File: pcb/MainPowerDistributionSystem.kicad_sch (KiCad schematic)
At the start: 12 parts, among them J2 PREC040DBAN-M71RC, U1 TPS22810DRV, U2 D24V7F5, U3 D24V7F3

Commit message: Renamed symbol and footprint `StackConnector` to `MainStackConnector`.
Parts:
- J1: footprint pcb:StackConnector -> pcb:MainStackConnector; symbol StackConnector:StackConnector -> MainStackConnector:MainStackConnector
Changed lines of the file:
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@@
 	)
 	(symbol
-		(lib_id "StackConnector:StackConnector")
+		(lib_id "MainStackConnector:MainStackConnector")
 		(at 461.01 69.85 0)
 		(unit 1)
@@
 			)
 		)
-		(property "Footprint" "pcb:StackConnector"
+		(property "Footprint" "pcb:MainStackConnector"
 			(at 459.74 69.85 0)
 			(effects

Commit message: Removed stepper motor drivers from `MainPowerDistributionSystem`.
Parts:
- removed JP1: Jumper_2_Bridged, Jumper:SolderJumper-2_P1.3mm_Open_RoundedPad1.0x1.5mm, symbol Jumper:Jumper_2_Bridged
- removed JP2: SolderJumper_2_Open, Jumper:SolderJumper-2_P1.3mm_Open_RoundedPad1.0x1.5mm, symbol Jumper:SolderJumper_2_Open
- removed R2: 1k, Resistor_SMD:R_1206_3216Metric_Pad1.30x1.75mm_HandSolder, symbol Device:R
- removed R3: 20k, Resistor_SMD:R_1206_3216Metric_Pad1.30x1.75mm_HandSolder, symbol Device:R
- removed TP1, TP2: TestPoint, TestPoint:TestPoint_Pad_1.0x1.0mm, symbol Connector:TestPoint
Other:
- removed sheet Stepper Motor Driver - X
- removed sheet Stepper Motor Driver - Y
- removed sheet Stepper Motor Driver - Z
- note removed: "@/pg 14/sec 3.4/`TMC2209`."
- note removed: "@/pg 20/fig 4.1/`TMC2209`."
- note removed: "Stepper Motor Drivers."
- note removed: "VREF is used for current scaling or something, but I don't think we'll need it; can be left floating according to example application diagram. @/pg 4/fig 1.1/`TMC2209`."
- moved on the sheet: J1, J2, R1, U1, U2, U3

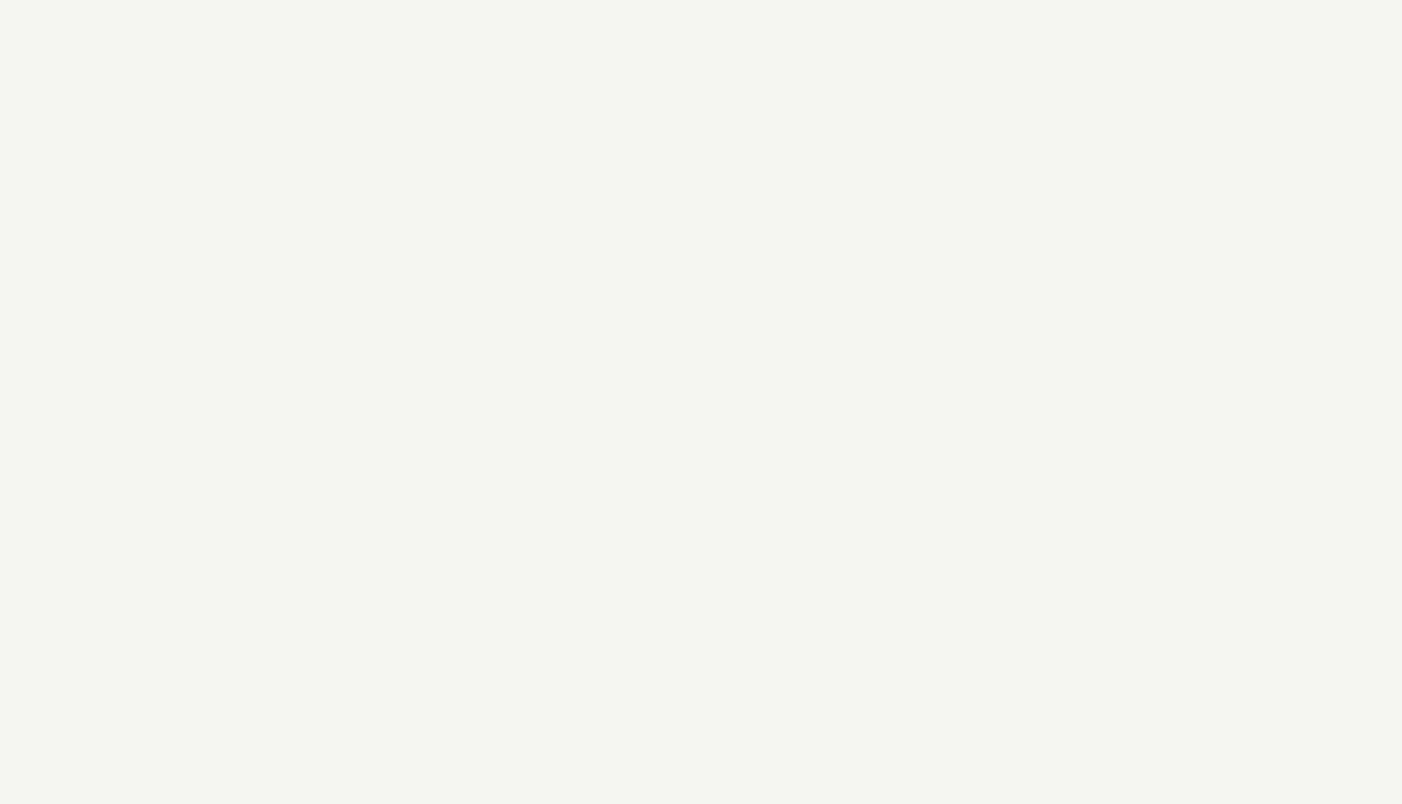
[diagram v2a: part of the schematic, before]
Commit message: Ported Maggie's schematic for timer event conversion.
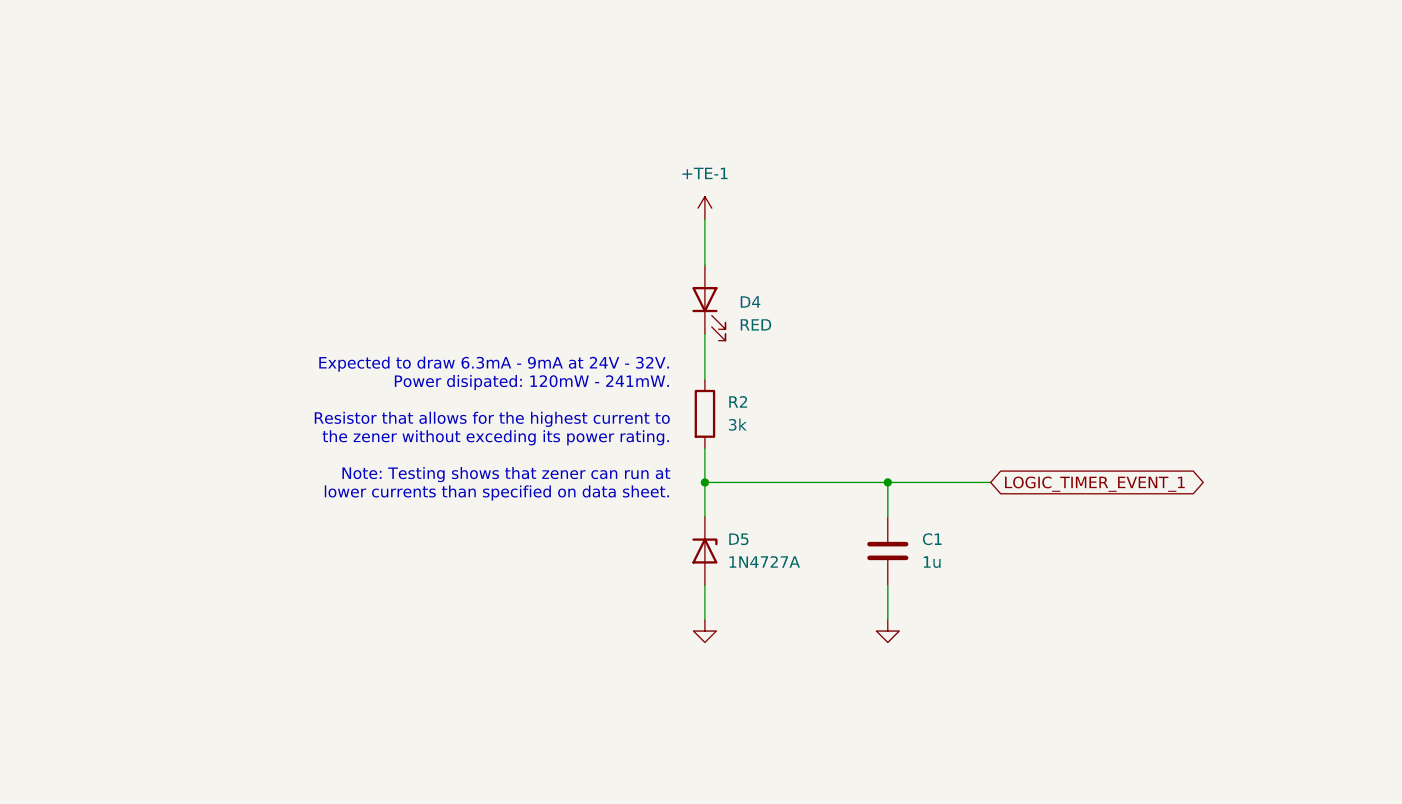
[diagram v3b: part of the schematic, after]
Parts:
- added C1: 1u, Capacitor_SMD:C_1206_3216Metric_Pad1.33x1.80mm_HandSolder, symbol Device:C
- added D4: RED, LED_SMD:LED_1206_3216Metric_Pad1.42x1.75mm_HandSolder, symbol Device:LED
- added D5: 1N4727A, Diode_THT:D_A-405_P7.62mm_Horizontal, symbol Device:D_Zener
- added R2: 3k, Resistor_SMD:R_1206_3216Metric_Pad1.30x1.75mm_HandSolder, symbol Device:R
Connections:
- net +TE-1: now also D4.2 (A)
- net GND: now also C1.2, D5.2 (A)
- new net: D4.1 (K), R2.1
- new net LOGIC_TIMER_EVENT_1: C1.1, D5.1 (K), R2.2
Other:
- note added: "Expected to draw 6.3mA - 9mA at 24V - 32V. Power disipated: 120mW - 241mW. Resistor that allows for the highest current to the zener without exceding its power rating. Note: Testing shows that zener can run at lower currents than specified on data sheet."

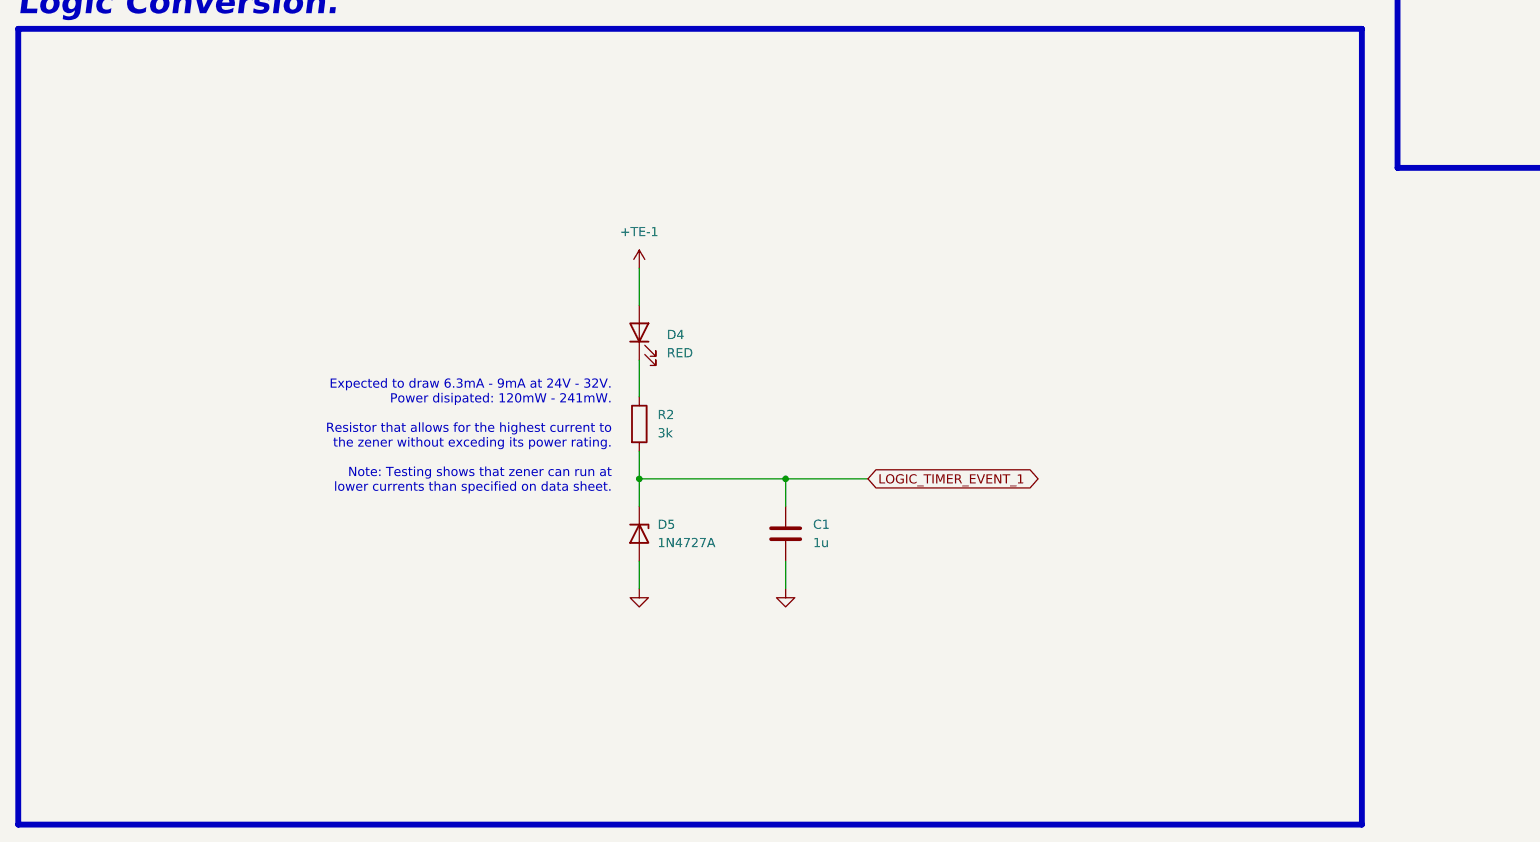
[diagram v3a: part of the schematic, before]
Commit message: Added the timer-event logic conversion stuff.
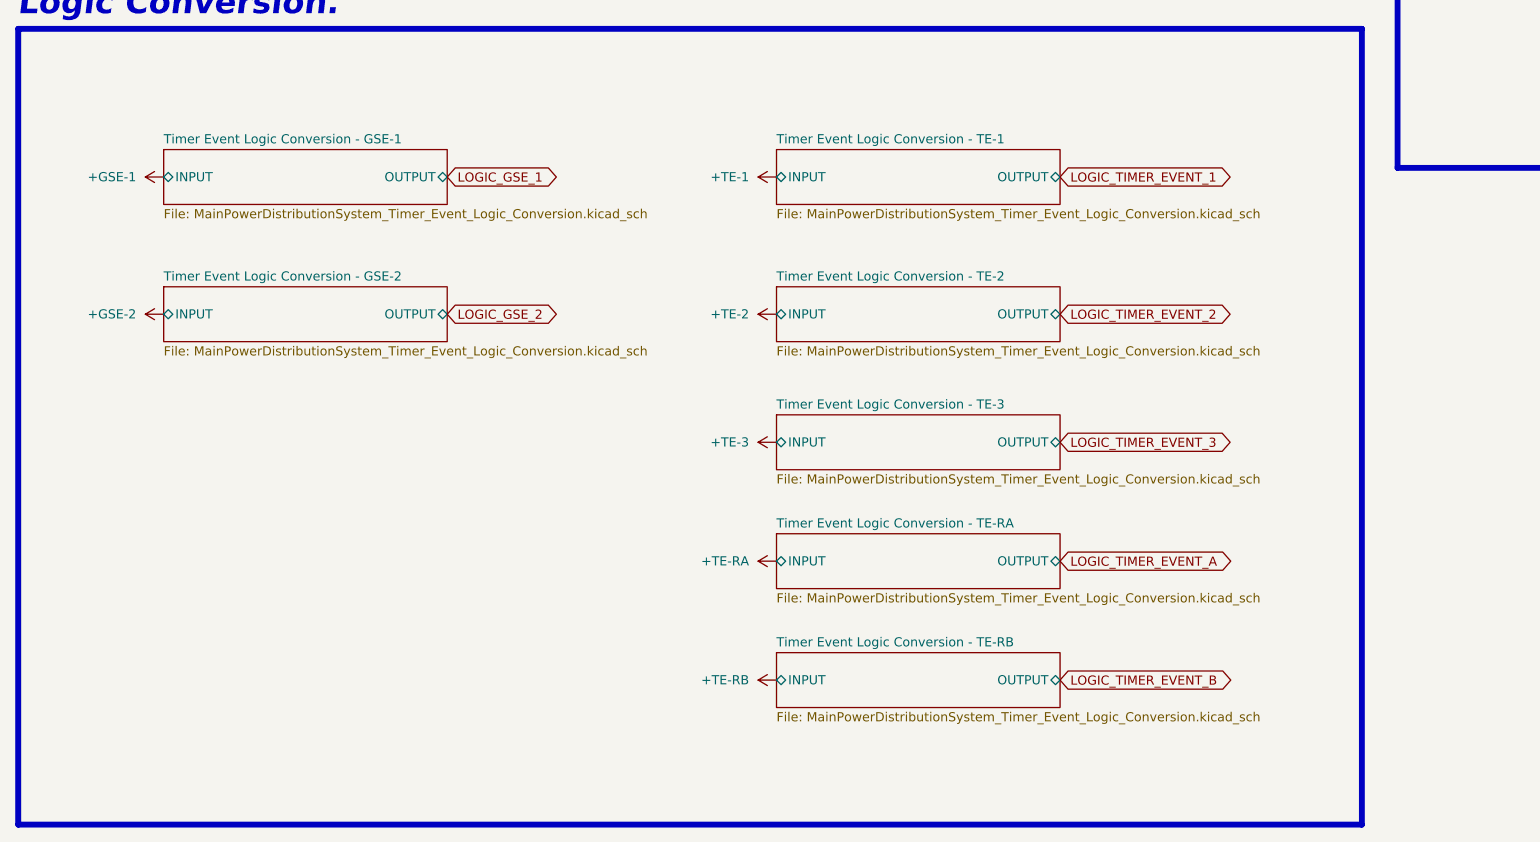
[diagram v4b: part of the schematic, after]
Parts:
- removed C1: 1u, Capacitor_SMD:C_1206_3216Metric_Pad1.33x1.80mm_HandSolder, symbol Device:C
- removed D4: RED, LED_SMD:LED_1206_3216Metric_Pad1.42x1.75mm_HandSolder, symbol Device:LED
- removed D5: 1N4727A, Diode_THT:D_A-405_P7.62mm_Horizontal, symbol Device:D_Zener
- removed R2: 3k, Resistor_SMD:R_1206_3216Metric_Pad1.30x1.75mm_HandSolder, symbol Device:R
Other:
- added sheet Timer Event Logic Conversion - GSE-1 (MainPowerDistributionSystem_Timer_Event_Logic_Conversion.kicad_sch)
- added sheet Timer Event Logic Conversion - GSE-2 (MainPowerDistributionSystem_Timer_Event_Logic_Conversion.kicad_sch)
- added sheet Timer Event Logic Conversion - TE-1 (MainPowerDistributionSystem_Timer_Event_Logic_Conversion.kicad_sch)
- added sheet Timer Event Logic Conversion - TE-2 (MainPowerDistributionSystem_Timer_Event_Logic_Conversion.kicad_sch)
- added sheet Timer Event Logic Conversion - TE-3 (MainPowerDistributionSystem_Timer_Event_Logic_Conversion.kicad_sch)
- added sheet Timer Event Logic Conversion - TE-RA (MainPowerDistributionSystem_Timer_Event_Logic_Conversion.kicad_sch)
- added sheet Timer Event Logic Conversion - TE-RB (MainPowerDistributionSystem_Timer_Event_Logic_Conversion.kicad_sch)
- note removed: "Expected to draw 6.3mA - 9mA at 24V - 32V. Power disipated: 120mW - 241mW. Resistor that allows for the highest current to the zener without exceding its power rating. Note: Testing shows that zener can run at lower currents than specified on data sheet."

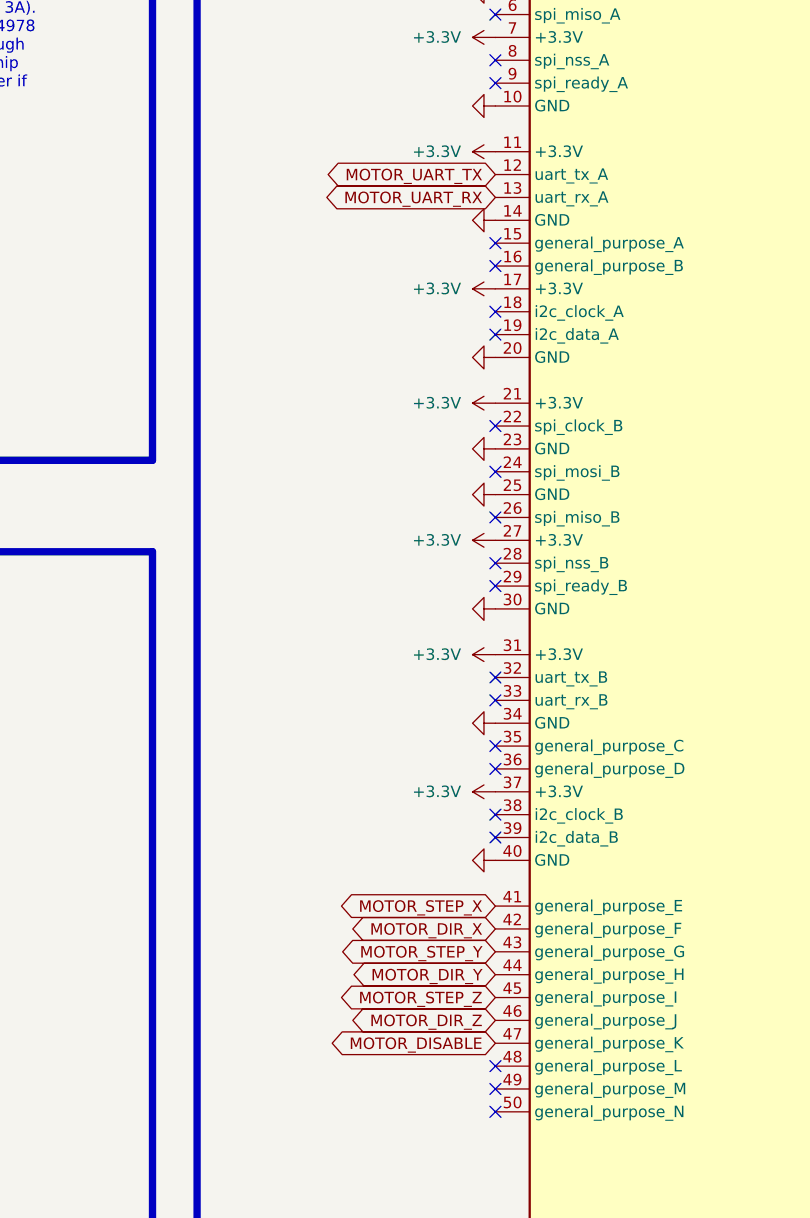
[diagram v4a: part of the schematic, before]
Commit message: Fixed issues reported by `checkPCBs` concerning the stack connectors.
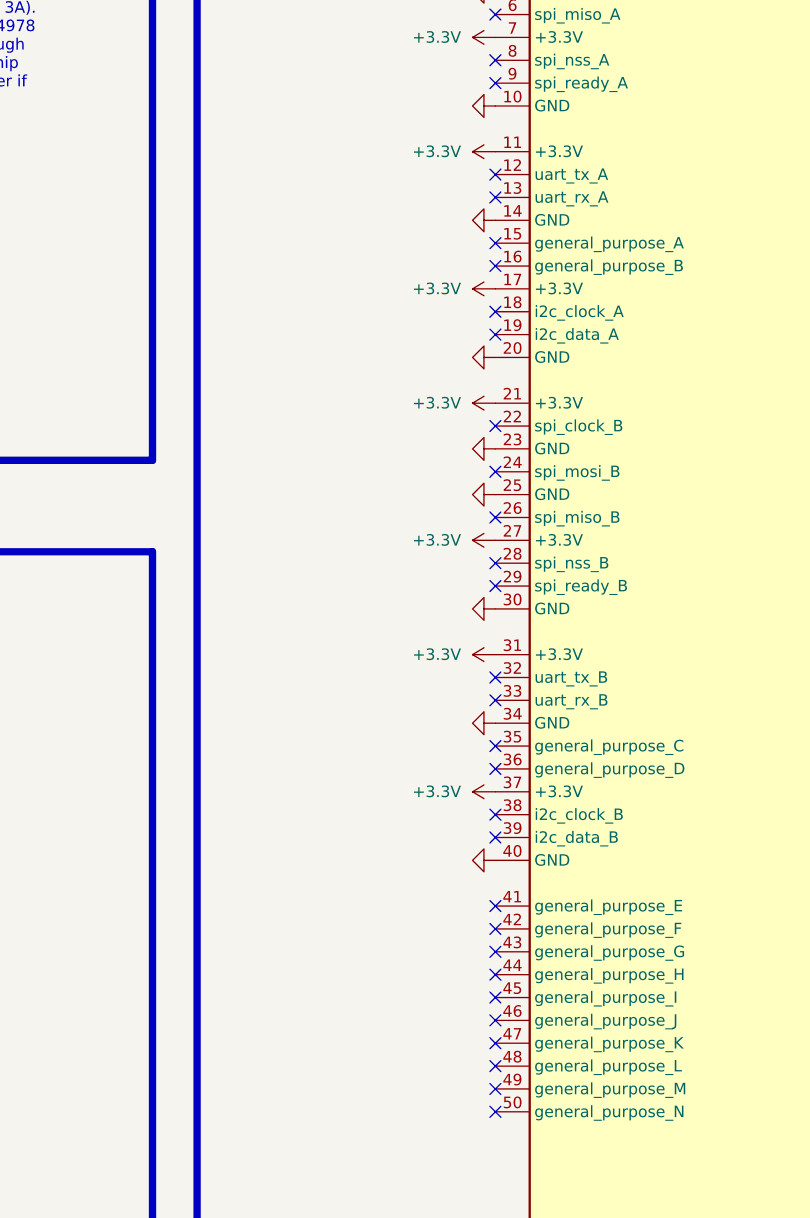
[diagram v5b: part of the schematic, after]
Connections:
- net MOTOR_DIR_X: no longer names the net of J1.42 (general_purpose_F)
- net MOTOR_DIR_Y: no longer names the net of J1.44 (general_purpose_H)
- net MOTOR_DIR_Z: no longer names the net of J1.46 (general_purpose_J)
- net MOTOR_DISABLE: no longer names the net of J1.47 (general_purpose_K)
- net MOTOR_STEP_X: no longer names the net of J1.41 (general_purpose_E)
- net MOTOR_STEP_Y: no longer names the net of J1.43 (general_purpose_G)
- net MOTOR_STEP_Z: no longer names the net of J1.45 (general_purpose_I)
- net MOTOR_UART_RX: no longer names the net of J1.13 (uart_rx_A)
- net MOTOR_UART_TX: no longer names the net of J1.12 (uart_tx_A)
- no-connect marks 77 -> 86
